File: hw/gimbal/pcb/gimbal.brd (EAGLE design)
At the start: 60 x 42 mm, 75 parts, among them J1 JST-XH4SMT_RA, U1 STM32F4R_64PIN, U2 TPS62172PWSON8, U3 TPS55330PQFN16, U4 MC33926, U5 DRV8313, U6 DRV8313, U7 AS5048A

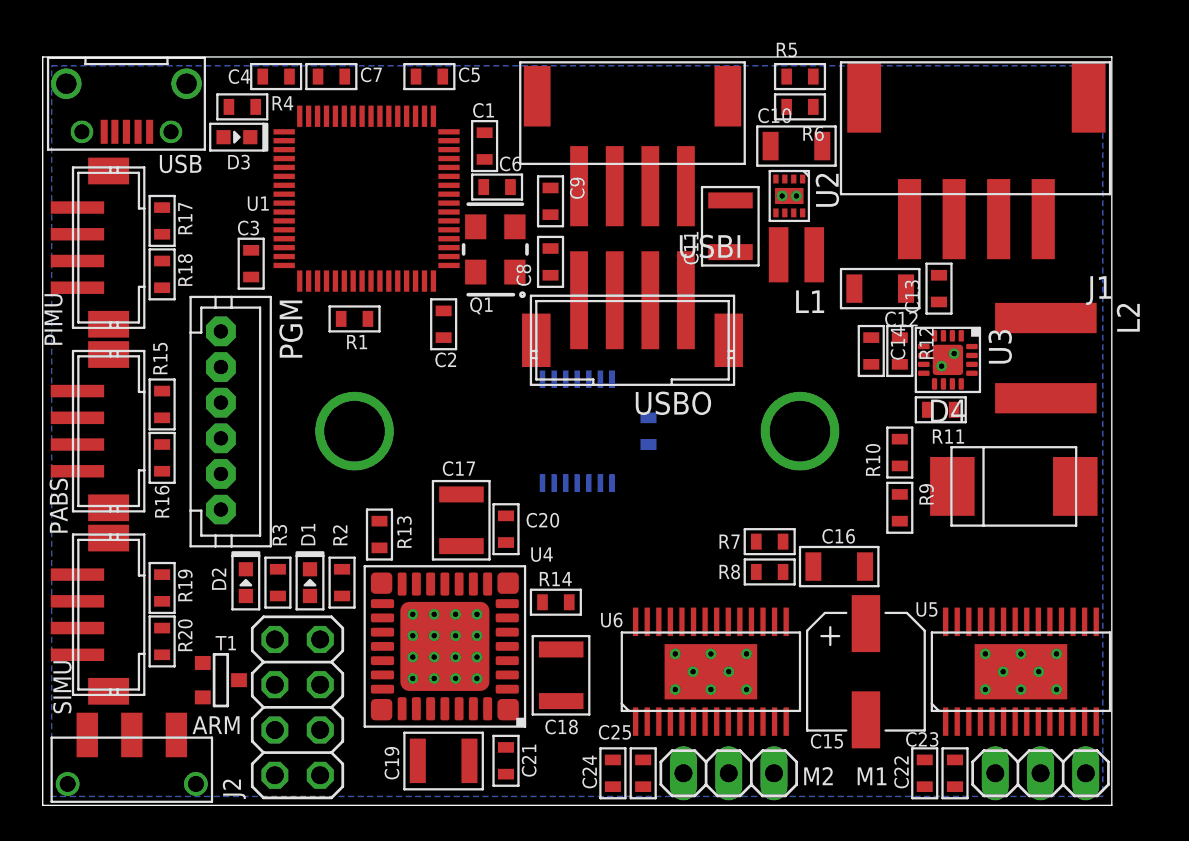
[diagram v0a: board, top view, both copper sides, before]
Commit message: gimbal board: First pass at all silks.
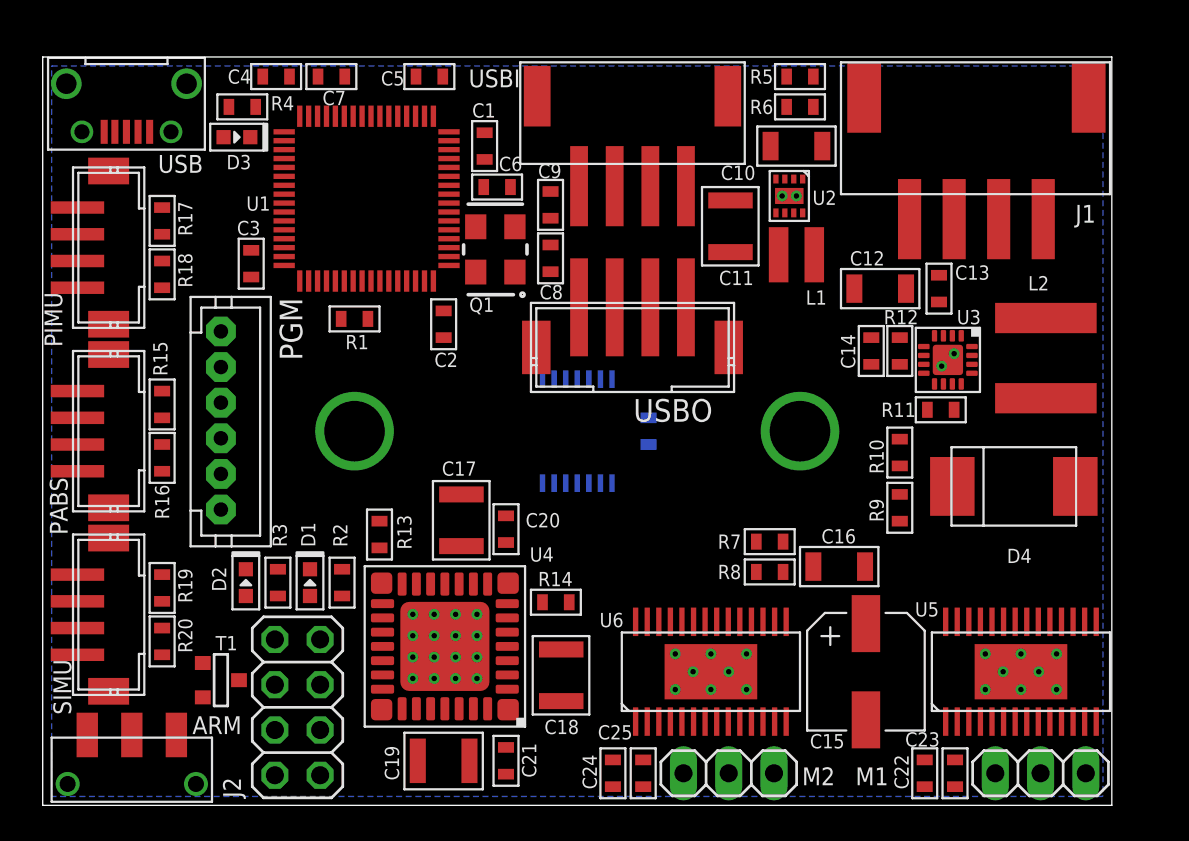
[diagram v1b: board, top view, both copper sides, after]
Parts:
- moved USBO 0.40 mm to (33.1, 26.2)
- moved C8 0.20 mm to (28.5, 30.7)
- moved C9 0.20 mm to (28.5, 33.7)

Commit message: gimbal board: Add test points for power rail, and an overall board label on the silk layer.
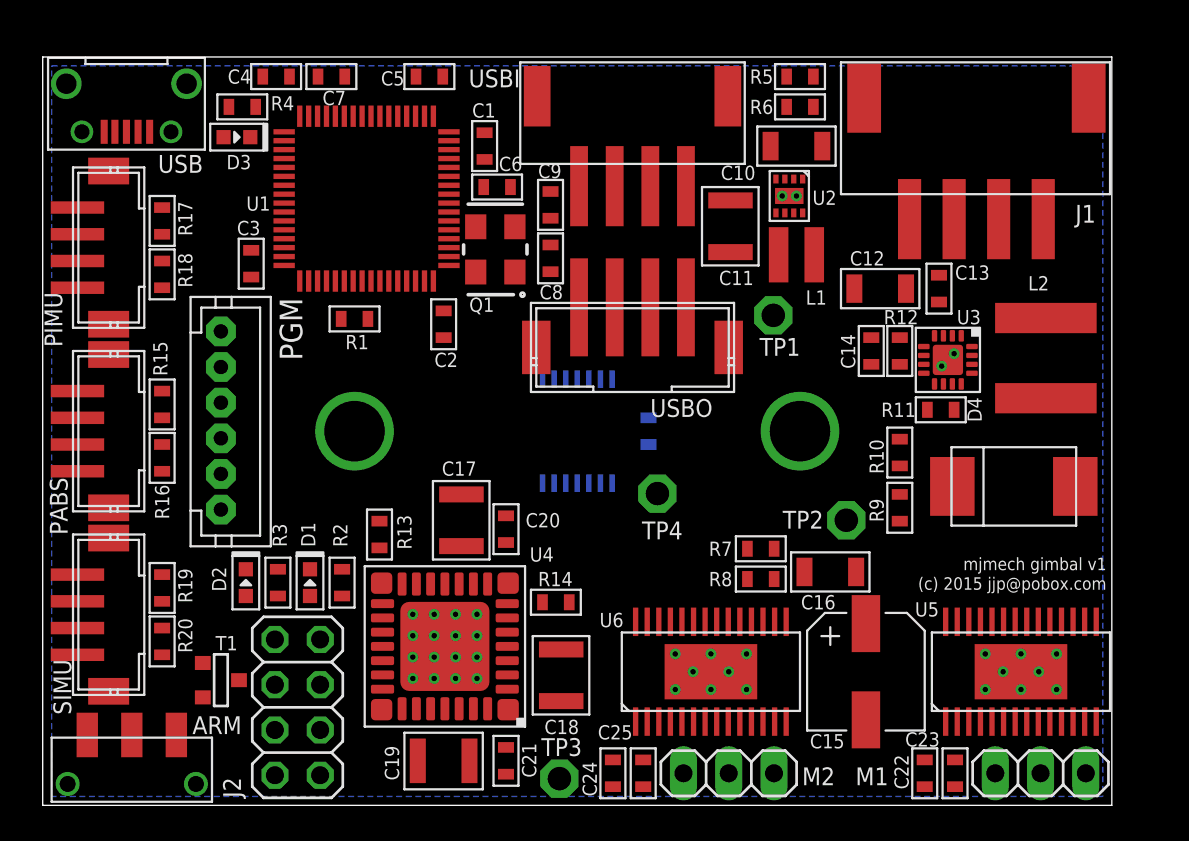
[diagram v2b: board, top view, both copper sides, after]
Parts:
- added TP1, TP2, TP3, TP4: TPPAD1-13, testpad:P1-13
- moved R7 0.64 mm to (40.3, 14.4)
- moved R8 0.64 mm to (40.3, 12.7)
- moved C16 0.58 mm to (44.2, 13.1)
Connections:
- net +12V: now also TP2.TP
- net +3V3: now also TP1.TP
- net +8V: now also TP3.TP
- net GND: now also TP4.TP
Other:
- board text added: "(c) 2015 jjp@pobox.com"
- board text added: "mjmech gimbal v1"

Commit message: gimbal board: Audited all package footprints and part values.  Fixed inconsistencies.
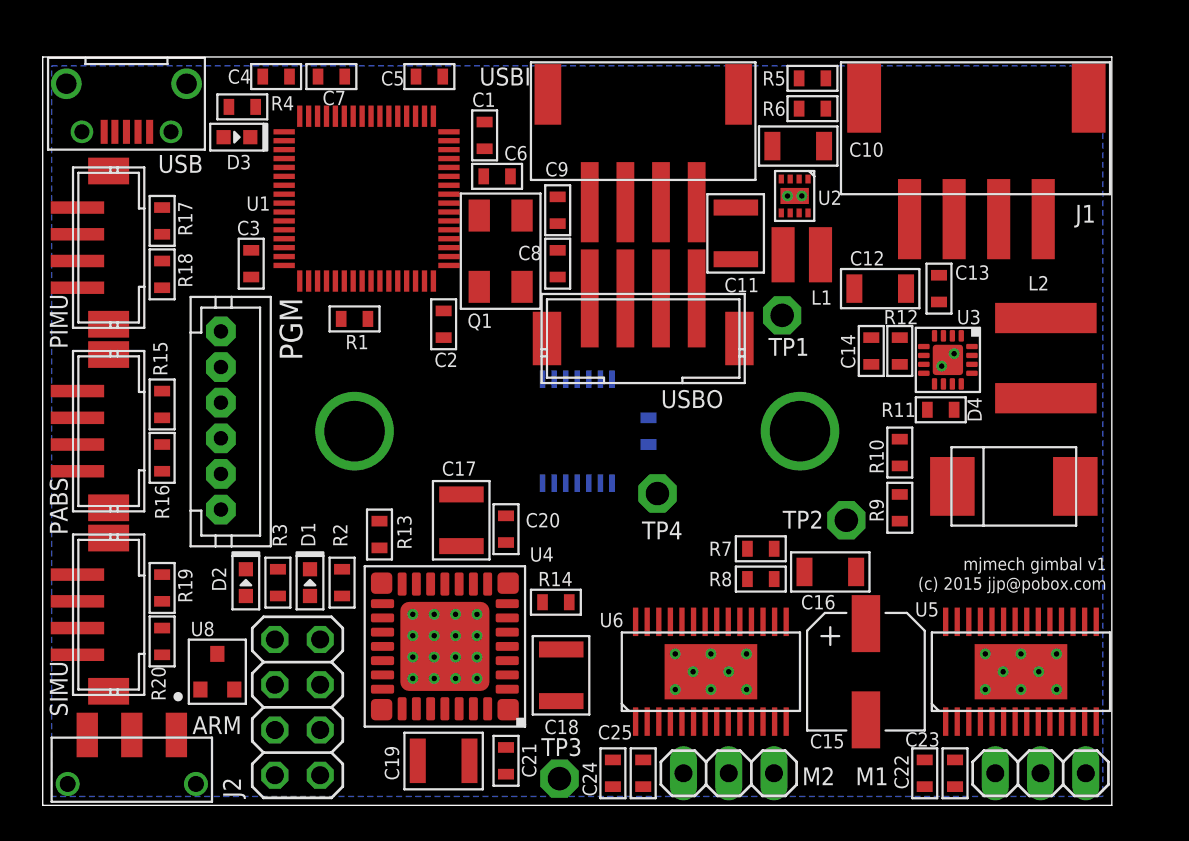
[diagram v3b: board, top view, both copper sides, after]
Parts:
- removed T1: (no value), zetex:SOT-23
- added U8: (no value), mfdiscrete:SOT-23-3
- Q1: device gimbal:CRYSTAL-OSC-SMD-5X3.2 -> gimbal:ABM3B
- moved USBI 1.08 mm to (33.7, 36.6)
- moved USBO 0.78 mm to (33.7, 26.7)
- moved R5 0.71 mm to (43.2, 40.8)
- moved R6 0.71 mm to (43.2, 39.1)
- moved C1 0.60 mm to (24.8, 37.6)
- moved C6 0.60 mm to (25.5, 35.3)
- moved C9 0.50 mm to (28.9, 33.4)
- moved TP1 0.50 mm to (41.5, 27.5)
- moved C8 0.50 mm to (28.9, 30.4)
- moved C11 0.50 mm to (38.9, 32.1)
- moved Q1 0.32 mm to (25.7, 31.1)
- moved L1 0.30 mm to (42.6, 30.9)
- moved U2 0.30 mm to (42.2, 34.2)
- moved C10 0.10 mm to (42.4, 37.0)
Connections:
- net GND: now also U8.P$2; no longer T1.2
- net LASER_EN: now also U8.P$1; no longer T1.3
- net N$1: now also U8.P$3; no longer T1.1

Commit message: gimbal board: WIP on power routing.
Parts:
- moved C12 3.50 mm to (50.5, 29.0), turned to 0 degrees
- moved C13 3.04 mm to (47.3, 28.5)
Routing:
- net +8V: track 0.00 -> 13.2 mm
- net N$21: track 0.00 -> 3.33 mm
- added copper zone on layer 1, net GND
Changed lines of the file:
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@@
 <attribute name="WATTAGE" value="N/A" x="48.1" y="25.5" size="1.778" layer="27" rot="R270" display="off"/>
 <attribute name="DPN" value="P1.87KHCT-ND" x="48.1" y="25.5" size="1.778" layer="27" rot="R270" display="off"/>
-<attribute name="NAME" x="47.2" y="27" size="0.8" layer="25" font="vector" ratio="10"/>
+<attribute name="NAME" x="48.8" y="24" size="0.8" layer="25" font="vector" ratio="10" rot="R180"/>
 </element>
 <element name="R9" library="mfpassives" package="R0603" value="88.7k" x="48.1" y="16.7" smashed="yes" rot="R270">
@@
 <attribute name="NAME" x="45.6" y="24.5" size="0.8" layer="25" font="vector" ratio="10" rot="R90"/>
 </element>
-<element name="C13" library="mfpassives" package="C0603" value="0.047uF" x="50.3" y="29" smashed="yes" rot="R90">
-<attribute name="TOLERANCE" value="N/A" x="50.3" y="29" size="1.778" layer="27" rot="R90" display="off"/>
-<attribute name="MFG#" value="N/A" x="50.3" y="29" size="1.778" layer="27" rot="R90" display="off"/>
-<attribute name="VOLTAGE" value="N/A" x="50.3" y="29" size="1.778" layer="27" rot="R90" display="off"/>
-<attribute name="TEMP_COF" value="N/A" x="50.3" y="29" size="1.778" layer="27" rot="R90" display="off"/>
-<attribute name="DPN" value="490-1522-1-ND" x="50.3" y="29" size="1.778" layer="27" rot="R90" display="off"/>
-<attribute name="NAME" x="51.2" y="29.5" size="0.8" layer="25" font="vector" ratio="10"/>
+<element name="C13" library="mfpassives" package="C0603" value="0.047uF" x="47.3" y="28.5" smashed="yes" rot="R90">
+<attribute name="TOLERANCE" value="N/A" x="47.3" y="28.5" size="1.778" layer="27" rot="R90" display="off"/>
+<attribute name="MFG#" value="N/A" x="47.3" y="28.5" size="1.778" layer="27" rot="R90" display="off"/>
+<attribute name="VOLTAGE" value="N/A" x="47.3" y="28.5" size="1.778" layer="27" rot="R90" display="off"/>
+<attribute name="TEMP_COF" value="N/A" x="47.3" y="28.5" size="1.778" layer="27" rot="R90" display="off"/>
+<attribute name="DPN" value="490-1522-1-ND" x="47.3" y="28.5" size="1.778" layer="27" rot="R90" display="off"/>
+<attribute name="NAME" x="45.7" y="30" size="0.8" layer="25" font="vector" ratio="10"/>
 </element>
 <element name="C16" library="mfpassives" package="C1206" value="10uF" x="44.2" y="13.1" smashed="yes" rot="R180">
@@
 <attribute name="NAME" x="47.2" y="37.2" size="0.8" layer="25" font="vector" ratio="10" rot="R180"/>
 </element>
-<element name="C12" library="mfpassives" package="C1206" value="10uF" x="47" y="29" smashed="yes" rot="R180">
-<attribute name="TOLERANCE" value="N/A" x="47" y="29" size="1.778" layer="27" rot="R180" display="off"/>
-<attribute name="MFG#" value="N/A" x="47" y="29" size="1.778" layer="27" rot="R180" display="off"/>
-<attribute name="VOLTAGE" value="N/A" x="47" y="29" size="1.778" layer="27" rot="R180" display="off"/>
-<attribute name="TEMP_COF" value="N/A" x="47" y="29" size="1.778" layer="27" rot="R180" display="off"/>
-<attribute name="AMFPN" value="MF-CAP-1206-10uF" x="47" y="29" size="1.778" layer="27" rot="R180" display="off"/>
-<attribute name="NAME" x="45.3" y="30.3" size="0.8" layer="25" font="vector" ratio="10"/>
+<element name="C12" library="mfpassives" package="C1206" value="10uF" x="50.5" y="29" smashed="yes">
+<attribute name="TOLERANCE" value="N/A" x="50.5" y="29" size="1.778" layer="27" display="off"/>
+<attribute name="MFG#" value="N/A" x="50.5" y="29" size="1.778" layer="27" display="off"/>
+<attribute name="VOLTAGE" value="N/A" x="50.5" y="29" size="1.778" layer="27" display="off"/>
+<attribute name="TEMP_COF" value="N/A" x="50.5" y="29" size="1.778" layer="27" display="off"/>
+<attribute name="AMFPN" value="MF-CAP-1206-10uF" x="50.5" y="29" size="1.778" layer="27" display="off"/>
+<attribute name="NAME" x="53" y="29.5" size="0.8" layer="25" font="vector" ratio="10"/>
 </element>
 <element name="C11" library="mfpassives" package="C1210" value="22uF 16V" x="38.9" y="32.1" smashed="yes" rot="R90">
@@
 <contactref element="TP4" pad="TP"/>
 <contactref element="U8" pad="P$2"/>
-<wire x1="50.3" y1="29.75" x2="56.15" y2="32.9" width="0" layer="19" extent="1-1"/>
-<wire x1="51.15" y1="25.35" x2="50.3" y2="29.75" width="0" layer="19" extent="1-1"/>
+<via x="55.1" y="33.6" extent="1-16" drill="0.32"/>
+<via x="55.1" y="32.7" extent="1-16" drill="0.32"/>
+<via x="55.1" y="31.8" extent="1-16" drill="0.32"/>
+<via x="55.1" y="30.9" extent="1-16" drill="0.32"/>
+<polygon width="0.4064" layer="1" thermals="no">
+<vertex x="55" y="34"/>
+<vertex x="55" y="30.8"/>
+<vertex x="56.5" y="30.8"/>
+<vertex x="56.5" y="34"/>
+</polygon>
+<wire x1="43.85" y1="37" x2="43.95" y2="39.1" width="0" layer="19" extent="1-1"/>
+<wire x1="42.95" y1="35.15" x2="43.85" y2="37" width="0" layer="19" extent="1-1"/>
+<wire x1="42.6" y1="34.2" x2="42.95" y2="35.15" width="0" layer="19" extent="1-1"/>
 <wire x1="42.2" y1="34.2" x2="41.8" y2="34.2" width="0" layer="19" extent="1-1"/>
 <wire x1="50.8" y1="25" x2="50.45" y2="24.65" width="0" layer="19" extent="1-1"/>
@@
 <wire x1="41.45" y1="33.25" x2="41.8" y2="34.2" width="0" layer="19" extent="1-1"/>
 <wire x1="41.45" y1="35.15" x2="41.8" y2="34.2" width="0" layer="19" extent="1-1"/>
-<wire x1="42.95" y1="35.15" x2="42.6" y2="34.2" width="0" layer="19" extent="1-1"/>
 <wire x1="50.55" y1="23.65" x2="50.45" y2="24.65" width="0" layer="19" extent="1-1"/>
 <wire x1="51.05" y1="23.65" x2="50.55" y2="23.65" width="0" layer="19" extent="1-1"/>
@@
 <wire x1="55.875" y1="10.3" x2="54.9" y2="8.5" width="0" layer="19" extent="1-1"/>
 <wire x1="38.475" y1="10.3" x2="37.5" y2="8.5" width="0" layer="19" extent="1-1"/>
-<wire x1="43.85" y1="37" x2="42.95" y2="35.15" width="0" layer="19" extent="1-1"/>
-<wire x1="43.95" y1="39.1" x2="43.85" y2="37" width="0" layer="19" extent="1-1"/>
 <wire x1="38.9" y1="33.55" x2="41.45" y2="33.25" width="0" layer="19" extent="1-1"/>
 <wire x1="59.125" y1="4.7" x2="56.525" y2="4.7" width="0" layer="19" extent="1-1"/>
@@
 <wire x1="42.75" y1="13.1" x2="41.05" y2="12.7" width="0" layer="19" extent="1-1"/>
 <wire x1="7.5" y1="3.95" x2="10.75" y2="6.5" width="0" layer="19" extent="1-1"/>
-<wire x1="45.55" y1="29" x2="46.5" y2="24.75" width="0" layer="19" extent="1-1"/>
+<wire x1="51.95" y1="29" x2="46.5" y2="24.75" width="0" layer="19" extent="1-1"/>
 <wire x1="48.1" y1="19.05" x2="51.15" y2="22.2" width="0" layer="19" extent="1-1"/>
 <wire x1="46.2" y1="4.8" x2="41.725" y2="4.7" width="0" layer="19" extent="1-1"/>
+<wire x1="47.3" y1="29.25" x2="51.15" y2="25.35" width="0" layer="19" extent="1-1"/>
 <wire x1="21.05" y1="2.5" x2="19.07" y2="6.52" width="0" layer="19" extent="1-1"/>
 <wire x1="26" y1="16.25" x2="24.37" y2="10.72" width="0" layer="19" extent="1-1"/>
@@
 <contactref element="C19" pad="P$1"/>
 <contactref element="TP3" pad="TP"/>
+<wire x1="48.65" y1="32.9" x2="49.05" y2="32.9" width="0.8128" layer="1"/>
+<wire x1="49.05" y1="32.9" x2="49.05" y2="29" width="0.8128" layer="1"/>
+<wire x1="49.05" y1="29" x2="51" y2="27.05" width="0.6096" layer="1"/>
+<wire x1="51" y1="27.05" x2="51" y2="27" width="0.4064" layer="1"/>
+<wire x1="51" y1="27" x2="51.05" y2="26.95" width="0.3048" layer="1"/>
+<wire x1="51.05" y1="26.95" x2="51.05" y2="26.35" width="0.3048" layer="1"/>
+<wire x1="56.3" y1="27.35" x2="51.45" y2="27.35" width="0.6096" layer="1"/>
+<wire x1="51.45" y1="27.35" x2="51.05" y2="26.95" width="0.6096" layer="1"/>
 <wire x1="40.95" y1="37" x2="43.95" y2="40.8" width="0" layer="19" extent="1-1"/>
 <wire x1="41.95" y1="35.15" x2="40.95" y2="37" width="0" layer="19" extent="1-1"/>
 <wire x1="42.45" y1="35.15" x2="41.95" y2="35.15" width="0" layer="19" extent="1-1"/>
 <wire x1="48.65" y1="32.9" x2="42.45" y2="35.15" width="0" layer="19" extent="1-1"/>
-<wire x1="48.45" y1="29" x2="48.65" y2="32.9" width="0" layer="19" extent="1-1"/>
-<wire x1="51.05" y1="26.35" x2="48.45" y2="29" width="0" layer="19" extent="1-1"/>
-<wire x1="56.3" y1="27.35" x2="51.05" y2="26.35" width="0" layer="19" extent="1-1"/>
 <wire x1="26" y1="14.75" x2="41.95" y2="35.15" width="0" layer="19" extent="1-1"/>
 <wire x1="23.5" y1="14.55" x2="26" y2="14.75" width="0" layer="19" extent="1-1"/>
@@
 <contactref element="U3" pad="4"/>
 <contactref element="C13" pad="P$1"/>
-<wire x1="50.05" y1="26.35" x2="50.3" y2="28.25" width="0" layer="19" extent="1-1"/>
+<wire x1="47.3" y1="27.75" x2="48.65" y2="27.75" width="0.3048" layer="1"/>
+<wire x1="48.65" y1="27.75" x2="50.05" y2="26.35" width="0.3048" layer="1"/>
 </signal>
 <signal name="N$22">
